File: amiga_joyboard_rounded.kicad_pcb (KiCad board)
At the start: 2 copper layers, 192.5 x 63.5 mm, 27 parts, among them J1 JOYPORT_OUT, J2 CONN_D, J3 CONN_F, SW1 FIRE_BTN, SW2 B_BTN, SW3 A_BTN, SW4 RIGHT_BTN, SW5 LEFT_BTN, SW6 DOWN_BTN, SW7 UP_BTN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

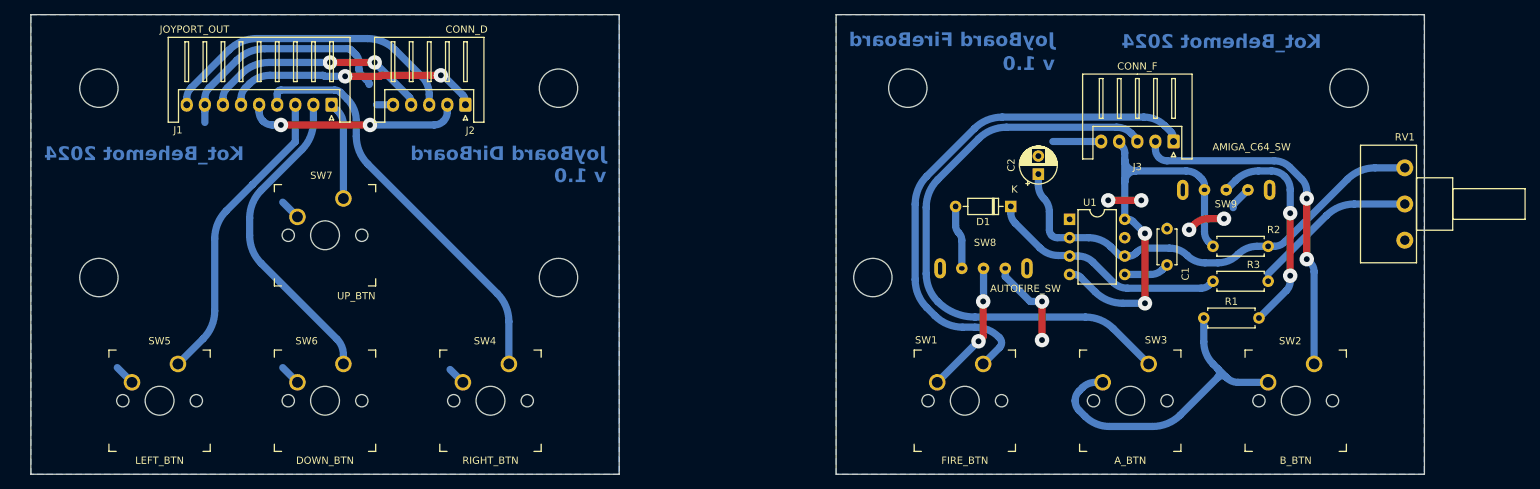
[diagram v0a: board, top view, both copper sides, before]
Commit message: footprints cleanup - kailh copied to local footprints dir
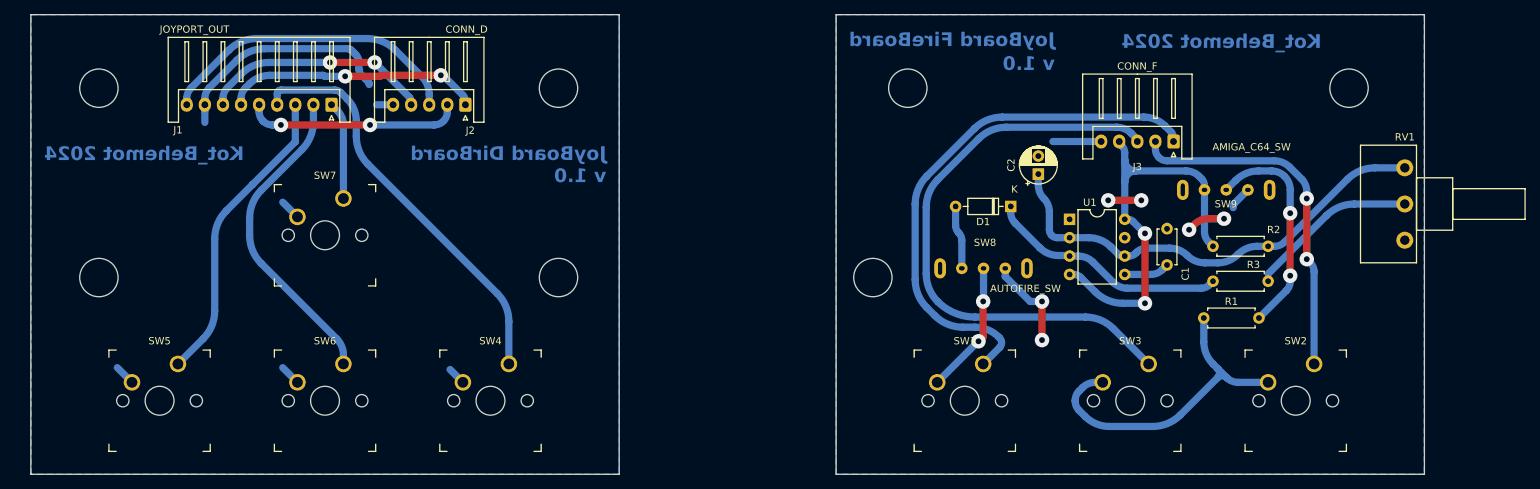
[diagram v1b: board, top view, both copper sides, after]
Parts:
- SW1, SW2, SW3, SW4, SW5, SW6, SW7: footprint Kailh:SW_MX -> Amiga Joyboard:SW_MX
